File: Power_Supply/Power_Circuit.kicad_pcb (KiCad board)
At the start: 2 copper layers, 142.2 x 102.9 mm, 49 parts, among them U1 B_Plug_5mm, U10 B_Plug_5mm, U11 B_Plug_5mm, U12 B_Plug_5mm, U13 B_Plug_5mm, U14 B_Plug_5mm, U15 DSN2596, U16 DSN2596, U17 B_Plug_5mm, U18 B_Plug_5mm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

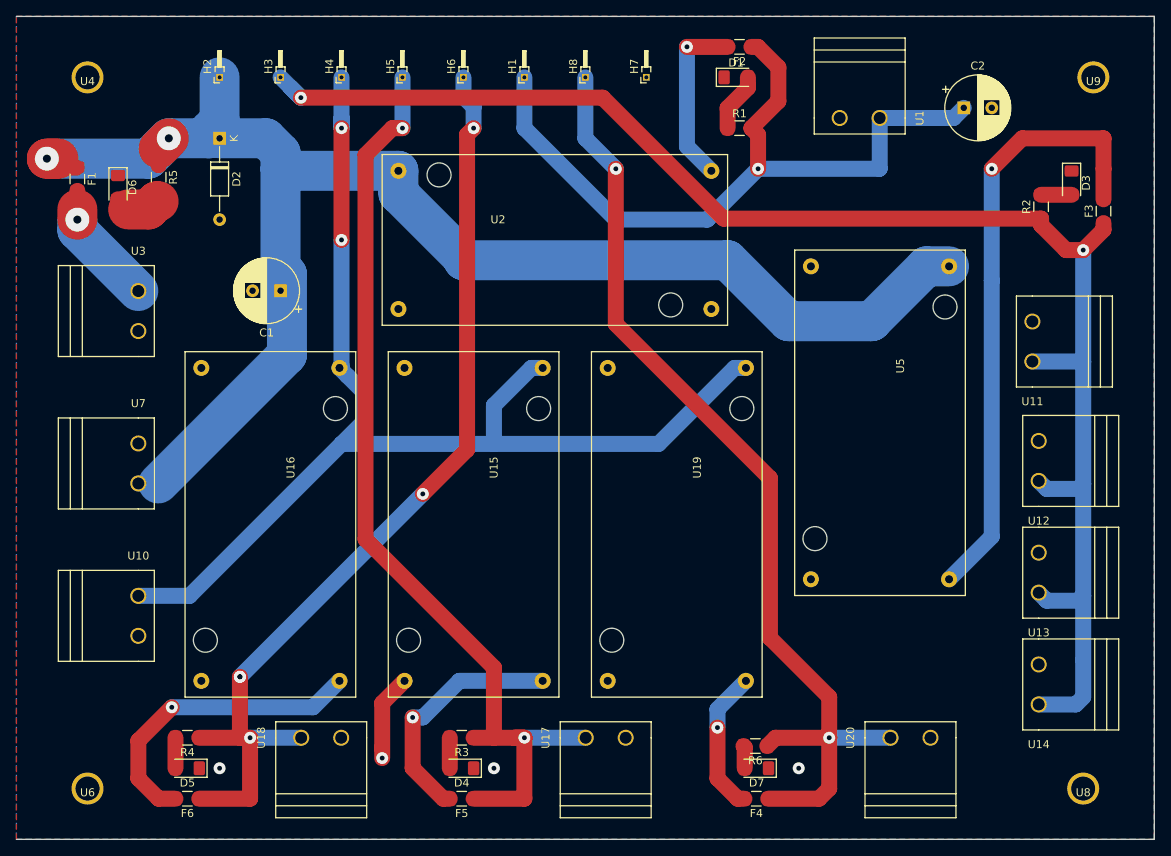
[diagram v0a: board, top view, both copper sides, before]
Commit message: Add electronic from 3A
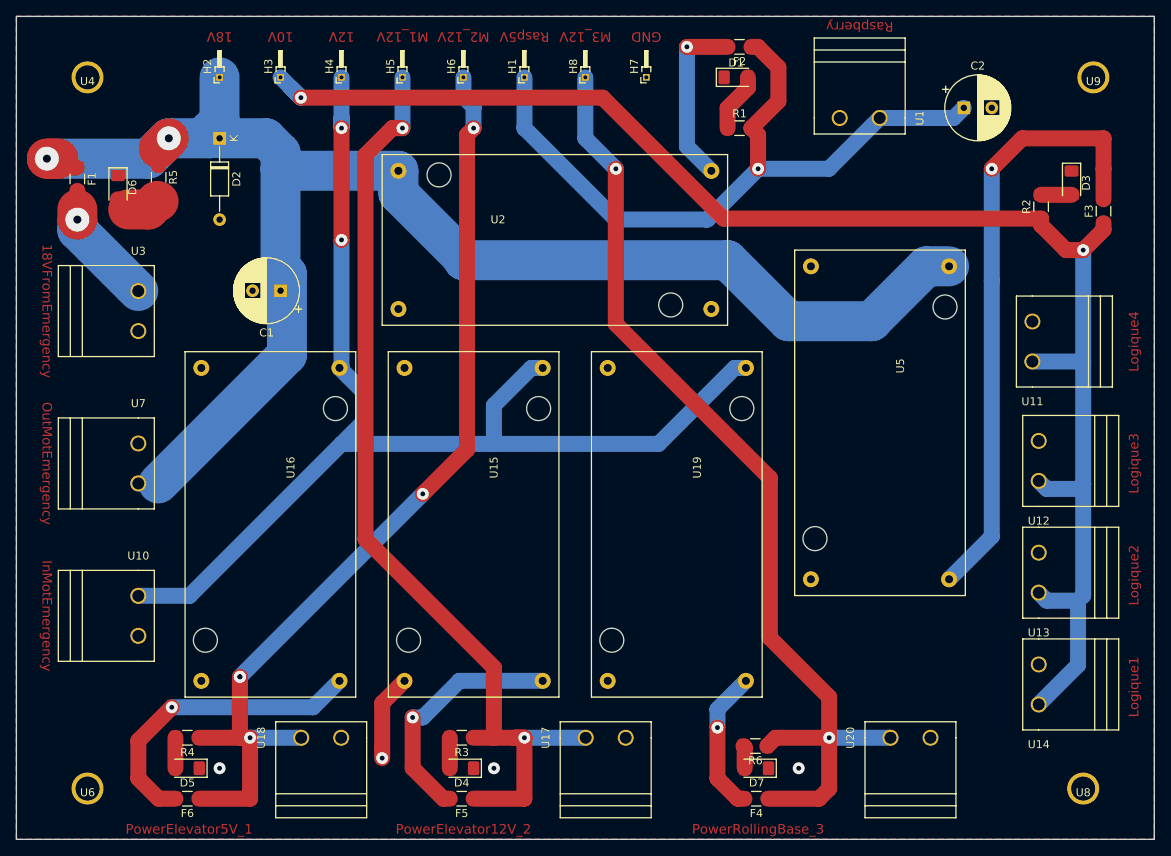
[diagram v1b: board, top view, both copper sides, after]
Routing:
- net Raspberr_5V: track 94.3 -> 90.6 mm
- net Logical_10V: track 198.4 -> 194.8 mm
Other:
- board text added: "10V"
- board text added: "12V"
- board text added: "18V"
- board text added: "18VFromEmergency"
- board text added: "GND"
- board text added: "InMotEmergency"
- board text added: "Logique1"
- board text added: "Logique2"
- board text added: "Logique3"
- board text added: "Logique4"
- board text added: "M1_12V"
- board text added: "M2_12V"
- board text added: "M3_12V"
- board text added: "OutMotEmergency"
- board text added: "PowerElevator12V_2"
- board text added: "PowerElevator5V_1"
- board text added: "PowerRollingBase_3"
- board text added: "Rasp5V"
- board text added: "Raspberry"
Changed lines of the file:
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@@
   (general
     (thickness 1.6)
-    (drawings 5)
-    (tracks 230)
+    (drawings 25)
+    (tracks 227)
     (zones 0)
     (modules 49)
@@
   )
   (setup
-    (last_trace_width 0.25)
+    (last_trace_width 2)
     (user_trace_width 2)
     (user_trace_width 3)
@@
       (drillshape 1)
       (scaleselection 1)
-      (outputdirectory ""))
+      (outputdirectory "../../../../Desktop/"))
   )
   (net 0 "")
@@
     (add_net "Net-(F6-Pad2)")
     (add_net Raspberr_5V)
+  )
+  (module "dsn2596:B plug 5mm" (layer F.Cu)
+    (at 139.219116 94.934906 180)
+    (fp_text reference U14 (at 0 -7.5 180) (layer F.SilkS)
+      (effects (font (size 1 1) (thickness 0.15)))
+    )
+    (fp_text value B_Plug_5mm (at 0 -9.5 180) (layer F.Fab)
+      (effects (font (size 1 1) (thickness 0.15)))
+    )
+    (fp_line (start -8.5 -5.685) (end -8.5 5.685) (layer F.SilkS) (width 0.15))
+    (fp_line (start -7 -5.685) (end -7 5.685) (layer F.SilkS) (width 0.15))
+    (fp_line (start -10 5.685) (end 0 5.685) (layer F.SilkS) (width 0.15))
+    (fp_line (start -10 -5.685) (end -10 5.685) (layer F.SilkS) (width 0.15))
+    (fp_line (start 0 -5.685) (end -10 -5.685) (layer F.SilkS) (width 0.15))
+    (fp_line (start 2 5.685) (end 0 5.685) (layer F.SilkS) (width 0.15))
+    (fp_line (start 2 -5.685) (end 2 5.685) (layer F.SilkS) (width 0.15))
+    (fp_line (start 0 -5.685) (end 2 -5.685) (layer F.SilkS) (width 0.15))
+    (fp_line (start 2 -5.685) (end 2 5.685) (layer F.SilkS) (width 0.15))
+    (pad 1 thru_hole circle (at 0 -2.5 180) (size 2 2) (drill 1.5) (layers *.Cu *.Mask F.SilkS)
+      (net 2 Logical_10V))
+    (pad 2 thru_hole circle (at 0 2.5 180) (size 2 2) (drill 1.5) (layers *.Cu *.Mask F.SilkS)
+      (net 1 GND))
   )
   (module dsn2596:DSN2596 (layer F.Cu)
@@
       (net 2 Logical_10V))
   )
-  (module "dsn2596:B plug 5mm" (layer F.Cu)
-    (at 139.219116 94.934906 180)
-    (fp_text reference U14 (at 0 -7.5 180) (layer F.SilkS)
-      (effects (font (size 1 1) (thickness 0.15)))
-    )
-    (fp_text value B_Plug_5mm (at 0 -9.5 180) (layer F.Fab)
-      (effects (font (size 1 1) (thickness 0.15)))
-    )
-    (fp_line (start -8.5 -5.685) (end -8.5 5.685) (layer F.SilkS) (width 0.15))
-    (fp_line (start -7 -5.685) (end -7 5.685) (layer F.SilkS) (width 0.15))
-    (fp_line (start -10 5.685) (end 0 5.685) (layer F.SilkS) (width 0.15))
-    (fp_line (start -10 -5.685) (end -10 5.685) (layer F.SilkS) (width 0.15))
-    (fp_line (start 0 -5.685) (end -10 -5.685) (layer F.SilkS) (width 0.15))
-    (fp_line (start 2 5.685) (end 0 5.685) (layer F.SilkS) (width 0.15))
-    (fp_line (start 2 -5.685) (end 2 5.685) (layer F.SilkS) (width 0.15))
-    (fp_line (start 0 -5.685) (end 2 -5.685) (layer F.SilkS) (width 0.15))
-    (fp_line (start 2 -5.685) (end 2 5.685) (layer F.SilkS) (width 0.15))
-    (pad 1 thru_hole circle (at 0 -2.5 180) (size 2 2) (drill 1.5) (layers *.Cu *.Mask F.SilkS)
-      (net 2 Logical_10V))
-    (pad 2 thru_hole circle (at 0 2.5 180) (size 2 2) (drill 1.5) (layers *.Cu *.Mask F.SilkS)
-      (net 1 GND))
-  )
   (module dsn2596:DSN2596 (layer F.Cu)
     (at 68.58 74.93 270)
@@
       (net 5 Motor2_12V))
   )
+  (gr_text Raspberry (at 116.84 12.7 180) (layer F.Cu)
+    (effects (font (size 1.2 1.2) (thickness 0.25)))
+  )
+  (gr_text InMotEmergency (at 15.24 86.36 270) (layer F.Cu)
+    (effects (font (size 1.2 1.2) (thickness 0.25)))
+  )
+  (gr_text OutMotEmergency (at 15.24 67.31 270) (layer F.Cu)
+    (effects (font (size 1.2 1.2) (thickness 0.25)))
+  )
+  (gr_text 18VFromEmergency (at 15.24 48.26 270) (layer F.Cu)
+    (effects (font (size 1.2 1.2) (thickness 0.25)))
+  )
+  (gr_text Logique4 (at 151.13 52.07 90) (layer F.Cu)
+    (effects (font (size 1.2 1.2) (thickness 0.25)))
+  )
+  (gr_text Logique3 (at 151.13 67.31 90) (layer F.Cu)
+    (effects (font (size 1.2 1.2) (thickness 0.25)))
+  )
+  (gr_text Logique2 (at 151.13 81.28 90) (layer F.Cu)
+    (effects (font (size 1.2 1.2) (thickness 0.25)))
+  )
+  (gr_text Logique1 (at 151.13 95.25 90) (layer F.Cu)
+    (effects (font (size 1.2 1.2) (thickness 0.25)))
+  )
+  (gr_text PowerRollingBase_3 (at 104.14 113.03) (layer F.Cu)
+    (effects (font (size 1.2 1.2) (thickness 0.25)))
+  )
+  (gr_text PowerElevator12V_2 (at 67.31 113.03) (layer F.Cu)
+    (effects (font (size 1.2 1.2) (thickness 0.25)))
+  )
+  (gr_text PowerElevator5V_1 (at 33.02 113.03) (layer F.Cu)
+    (effects (font (size 1.2 1.2) (thickness 0.25)))
+  )
+  (gr_text GND (at 90.17 13.97 180) (layer F.Cu)
+    (effects (font (size 1.2 1.2) (thickness 0.25)))
+  )
+  (gr_text M3_12V (at 82.55 13.97 180) (layer F.Cu)
+    (effects (font (size 1.2 1.2) (thickness 0.25)))
+  )
+  (gr_text Rasp5V (at 74.93 13.97 180) (layer F.Cu)
+    (effects (font (size 1.2 1.2) (thickness 0.25)))
+  )
+  (gr_text M2_12V (at 67.31 13.97 180) (layer F.Cu)
+    (effects (font (size 1.2 1.2) (thickness 0.25)))
+  )
+  (gr_text "M1_12V\n" (at 59.69 13.97 180) (layer F.Cu)
+    (effects (font (size 1.2 1.2) (thickness 0.25)))
+  )
+  (gr_text 12V (at 52.07 13.97 180) (layer F.Cu)
+    (effects (font (size 1.2 1.2) (thickness 0.25)))
+  )
+  (gr_text 10V (at 44.45 13.97 180) (layer F.Cu)
+    (effects (font (size 1.2 1.2) (thickness 0.25)))
+  )
+  (gr_line (start 11.43 114.3) (end 11.43 11.43) (layer Edge.Cuts) (width 0.1))
+  (gr_text 18V (at 36.83 13.97 180) (layer F.Cu)
+    (effects (font (size 1.2 1.2) (thickness 0.25)))
+  )
   (gr_line (start 153.67 114.3) (end 11.43 114.3) (layer Edge.Cuts) (width 0.1))
   (gr_line (start 153.67 11.43) (end 153.67 114.3) (layer Edge.Cuts) (width 0.1))
@@
   (segment (start 144.78 40.64) (end 144.78 40.64) (width 2) (layer F.Cu) (net 2))
   (via (at 144.78 40.64) (size 1.5) (drill 0.6) (layers F.Cu B.Cu) (net 2))
-  (segment (start 139.219116 97.434906) (end 143.865094 97.434906) (width 2) (layer B.Cu) (net 2))
-  (segment (start 144.78 96.52) (end 144.78 91.874022) (width 2) (layer B.Cu) (net 2))
-  (segment (start 143.865094 97.434906) (end 144.78 96.52) (width 2) (layer B.Cu) (net 2))
   (segment (start 144.135095 84.464905) (end 144.78 83.82) (width 2) (layer B.Cu) (net 2))
   (segment (start 140.219115 84.464905) (end 144.135095 84.464905) (width 2) (layer B.Cu) (net 2))
   (segment (start 139.219116 83.464906) (end 140.219115 84.464905) (width 2) (layer B.Cu) (net 2))
-  (segment (start 144.78 83.82) (end 144.78 91.874022) (width 2) (layer B.Cu) (net 2))
   (segment (start 144.135095 70.494905) (end 144.78 69.85) (width 2) (layer B.Cu) (net 2))
   (segment (start 140.219115 70.494905) (end 144.135095 70.494905) (width 2) (layer B.Cu) (net 2))
@@
   (segment (start 46.99 21.59) (end 84.713998 21.59) (width 2) (layer F.Cu) (net 2))
   (segment (start 84.713998 21.59) (end 99.829597 36.705599) (width 2) (layer F.Cu) (net 2))
+  (segment (start 144.135095 92.518927) (end 139.219116 97.434906) (width 2) (layer B.Cu) (net 2))
+  (segment (start 144.135095 84.464905) (end 144.135095 92.518927) (width 2) (layer B.Cu) (net 2))
   (segment (start 54.808001 58.364001) (end 52.815999 56.371999) (width 2) (layer B.Cu) (net 3))
   (segment (start 52.815999 56.371999) (end 51.816 55.372) (width 2) (layer B.Cu) (net 3))
@@
   (segment (start 104.1175 15.24) (end 103.305 15.24) (width 2) (layer F.Cu) (net 14))
   (segment (start 106.68 22.025) (end 106.68 17.8025) (width 2) (layer F.Cu) (net 14))
-  (segment (start 119.34 24.13) (end 119.34 30.44) (width 2) (layer B.Cu) (net 14))
-  (segment (start 119.34 30.44) (end 119.3 30.48) (width 2) (layer B.Cu) (net 14))
-  (segment (start 119.3 30.48) (end 104.14 30.48) (width 2) (layer B.Cu) (net 14))
   (segment (start 104.14 30.48) (end 104.14 30.48) (width 2) (layer B.Cu) (net 14))
   (via (at 104.14 30.48) (size 1.5) (drill 0.6) (layers F.Cu B.Cu) (net 14))
@@
   (segment (start 86.36 36.83) (end 74.93 25.4) (width 2) (layer B.Cu) (net 14))
   (segment (start 74.93 25.4) (end 74.93 19.05) (width 2) (layer B.Cu) (net 14))
+  (segment (start 112.99 30.48) (end 119.34 24.13) (width 2) (layer B.Cu) (net 14))
+  (segment (start 104.14 30.48) (end 112.99 30.48) (width 2) (layer B.Cu) (net 14))
   (segment (start 102.47 102.79) (end 102.315001 102.635001) (width 2) (layer F.Cu) (net 15))
   (segment (start 102.47 105.41) (end 102.47 102.79) (width 2) (layer F.Cu) (net 15))
